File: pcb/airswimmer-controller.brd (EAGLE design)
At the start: 29 x 27 mm, 49 parts, among them M1+ SOLDER_PAD.05X.05, M1- SOLDER_PAD.05X.05, M2+ SOLDER_PAD.05X.05, M2- SOLDER_PAD.05X.05, Y1 16MHz

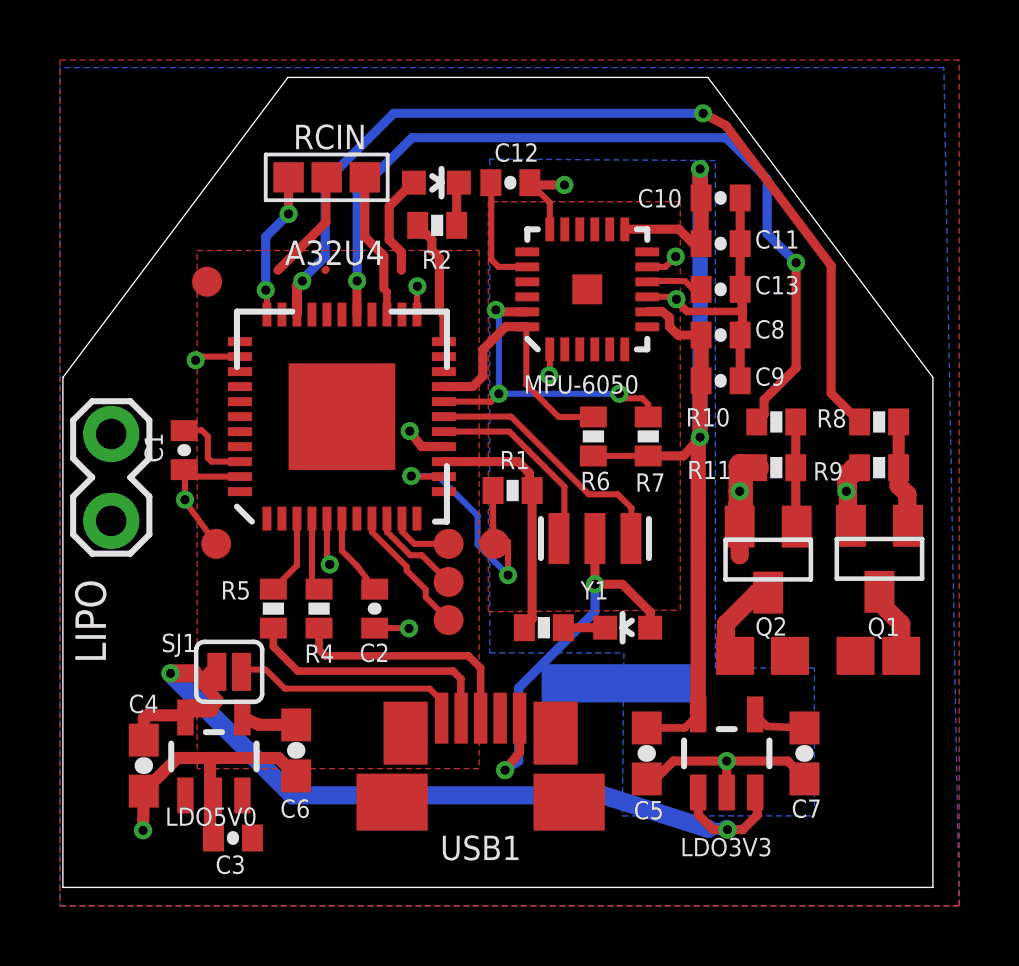
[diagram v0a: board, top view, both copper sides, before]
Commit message: Correct LED cathode direction in schematic and board.
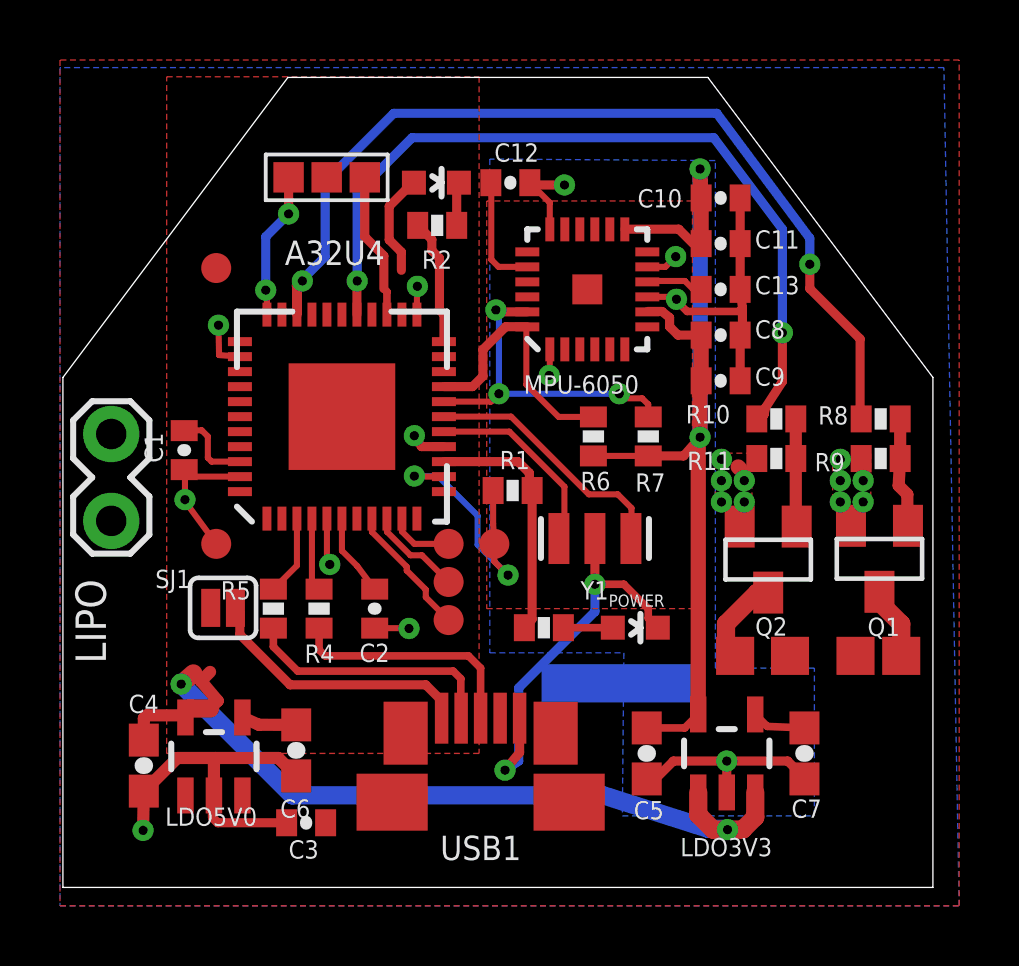
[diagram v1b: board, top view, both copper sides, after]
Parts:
- removed LED2: Green, SparkFun-LED:LED-0603
- added POWER: Green, SparkFun-LED:LED-0603
- moved C3 2.49 mm to (44.3, 38.8)
- moved SJ1 2.14 mm to (41.5, 46.0)
- moved VCC 0.55 mm to (41.3, 57.3)
- moved R9 0.31 mm to (63.4, 51.0)
- moved R11 0.30 mm to (59.9, 51.0)
- moved R8 0.11 mm to (63.4, 52.3)
- moved R10 0.10 mm to (59.9, 52.3)
- renumbered LED1 to STATUS
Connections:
- net GND: now also POWER.C; no longer LED2.A
- net N$10: now also POWER.A; no longer LED2.C
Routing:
- net GND: track 48.9 -> 42.2 mm, vias 13 -> 21
- net VCC: track 46.1 -> 41.3 mm
- net UVCC: track 7.71 -> 9.17 mm
- net MOT2: track 28.1 -> 27.2 mm
- added copper zone on layer 1, net GND
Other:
- board text added: "- + S"
- board text added: "V0.1 Air Swimmer Controller 10-Apr-2013"
- board text removed: "Air Swimmer Controller V0.1 10-Apr-2013"
